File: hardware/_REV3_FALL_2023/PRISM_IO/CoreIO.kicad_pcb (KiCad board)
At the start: 2 copper layers, 61 x 88.9 mm, 39 parts, among them J1 CORE_FC, J2 COTS_SWITCH_PLUG, J3 PYRO 1, J4 PYRO 2, Q1 AO3400A, Q2 AO3400A

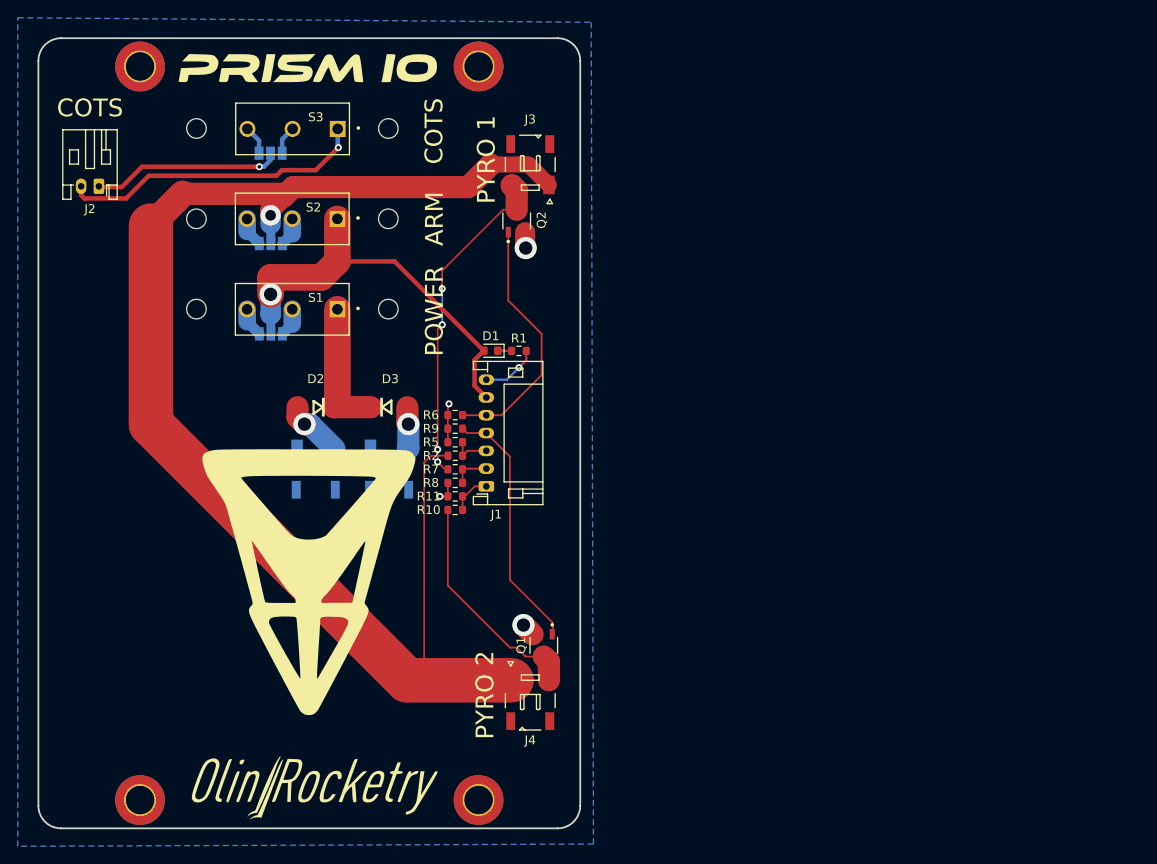
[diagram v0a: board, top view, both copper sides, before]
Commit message: update Core IO schematic and first layout concept
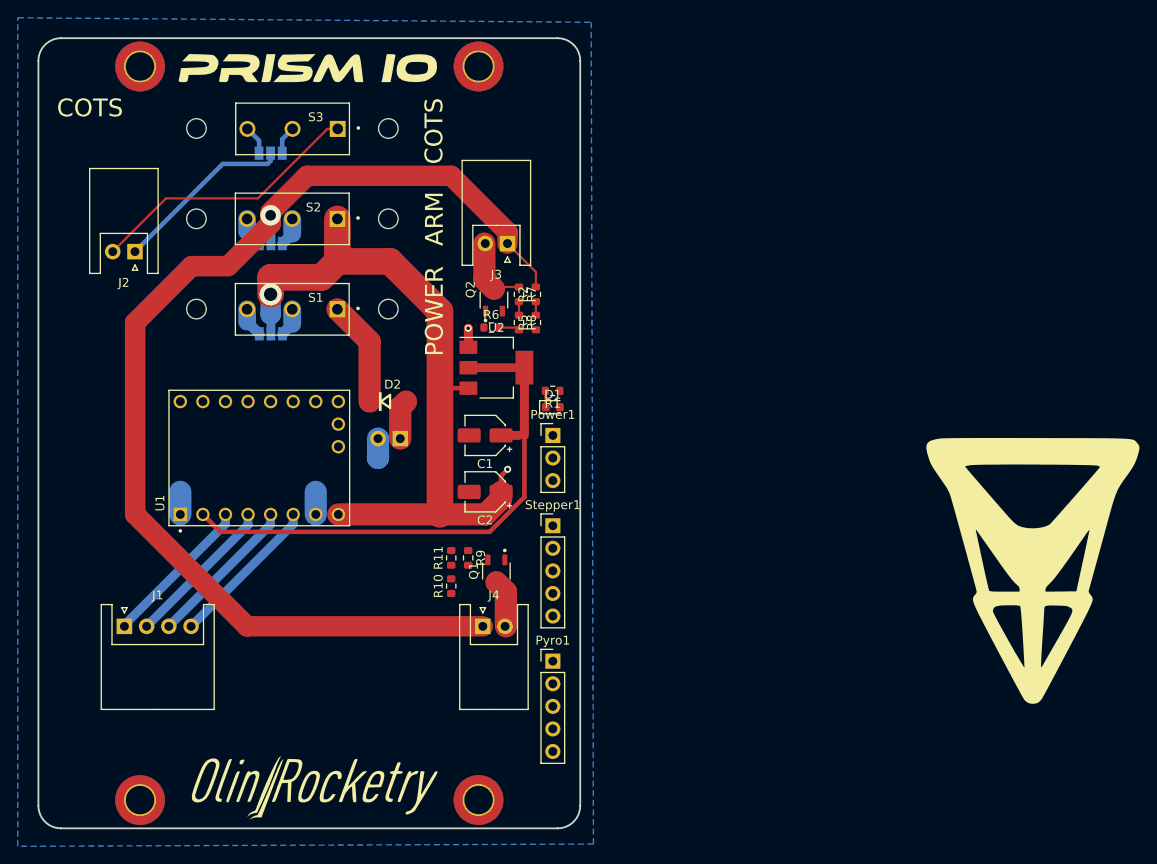
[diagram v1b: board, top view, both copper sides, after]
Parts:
- removed BT2: ~, JST:JST_SFH_SM02B-SFHRS-TF_02x1.80mm_Angled
- removed D3: SS54, JLC_footprints:DO-214AC
- added C1: 10uF, Capacitor_SMD:CP_Elec_4x5.4, F.Cu at (167.6, 95.2)
- added C2: 10uF, Capacitor_SMD:CP_Elec_4x5.4, F.Cu at (167.6, 101.6)
- added Power1: Conn_01x03_Socket, Connector_PinHeader_2.54mm:PinHeader_1x03_P2.54mm_Vertical, F.Cu at (175.3, 95.2)
- added Pyro1: Conn_01x05_Socket, Connector_PinHeader_2.54mm:PinHeader_1x05_P2.54mm_Vertical, F.Cu at (175.3, 120.7)
- added Stepper1: Conn_01x05_Socket, Connector_PinHeader_2.54mm:PinHeader_1x05_P2.54mm_Vertical, F.Cu at (175.3, 105.4)
- added U1: TMC2209_SILENTSTEPSTICK, TMC2209_SILENTSTEPSTICK:MODULE_TMC2209_SILENTSTEPSTICK, F.Cu at (142.2, 97.8)
- added U2: LD1117S12TR_SOT223, Package_TO_SOT_SMD:SOT-223-3_TabPin2, F.Cu at (168.9, 87.6)
- BT1, J3, J4: footprint JST:JST_SFH_SM02B-SFHRS-TF_02x1.80mm_Angled -> Connectors_JST.pretty-master:JST_XH_S02B-XH-A_02x2.50mm_Angled
- J1: value CORE_FC -> Conn_01x04_Socket; footprint Connector_JST:JST_PH_S7B-PH-K_1x07_P2.00mm_Horizontal -> Connectors_JST.pretty-master:JST_XH_S04B-XH-A_04x2.50mm_Angled
- J2: footprint Connector_JST:JST_PH_S2B-PH-K_1x02_P2.00mm_Horizontal -> Connectors_JST.pretty-master:JST_XH_S02B-XH-A_02x2.50mm_Angled
- Q2: footprint AO3400A:SOT95P280X125-3N -> AO3400A.pretty-master:SOT95P280X125-3N
- R1: value 150 -> 1k
- R10: value 10k -> 56K
- R11, R8: value 10k -> 15K
- R2: value 10k -> 56k
- R5: value 10k -> 15k
- moved G*** 81.5 mm to (229.2, 110.5)
- moved J1 43.7 mm to (127.1, 116.7), turned to 0 degrees
- moved R7 21.0 mm to (171.4, 79.4), turned to -90 degrees
- moved R2 20.3 mm to (173.4, 79.4), turned to 90 degrees
- moved R8 19.4 mm to (171.4, 82.5), turned to -90 degrees
- moved R5 16.2 mm to (173.4, 82.5), turned to 90 degrees
- moved R9 14.6 mm to (165.7, 109.0), turned to -90 degrees
- moved R6 10.7 mm to (168.3, 83.1), turned to 0 degrees
- moved BT1 10.1 mm to (158.1, 95.6)
- moved J4 9.92 mm to (167.4, 116.7)
- moved Q1 9.92 mm to (168.9, 110.5)
- moved D1 9.43 mm to (175.3, 92.1), turned to 0 degrees
- moved J3 9.25 mm to (170.2, 73.7)
- moved Q2 9.25 mm to (168.6, 80.0)
- moved R10 8.58 mm to (163.8, 112.2), turned to 90 degrees
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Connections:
- J1 pad 1: /CONT 2 -> Net-(J1-Pin_1)
- J1 pad 2: /CONT 1 -> Net-(J1-Pin_2)
- J1 pad 3: /ARM -> Net-(J1-Pin_3)
- J1 pad 4: /PYRO 2 -> Net-(J1-Pin_4)
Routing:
- net /5V: track 0.00 -> 62.1 mm
- net /V_BATT: track 46.0 -> 81.8 mm, vias 1 -> 2
- net /V_IGNITOR: track 159.4 -> 128.7 mm
- net Net-(J3-Pin_2): track 37.5 -> 8.44 mm, vias 4 -> 0
- net /PYRO 2: track 28.6 -> 0.00 mm
- net /PYRO 1: track 28.4 -> 0.25 mm
- net Net-(J4-Pin_2): track 25.5 -> 5.41 mm
- net Net-(J1-Pin_4): track 0.00 -> 17.3 mm
- net Net-(J1-Pin_3): track 0.00 -> 17.3 mm
- net Net-(J1-Pin_2): track 0.00 -> 17.3 mm
- net Net-(J1-Pin_1): track 0.00 -> 17.3 mm
- net GND: track 16.8 -> 11.8 mm, vias 5 -> 1
- net Net-(BT2-Pad1): track 4.75 -> 0.00 mm, vias 1 -> 0
- net /CONT 2: track 4.67 -> 0.00 mm
- net Net-(J2-Pin_2): track 34.6 -> 31.0 mm, vias 1 -> 0
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
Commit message: fixed stepper wiring
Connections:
- U1 pad 16: unconnected-(U1-~{EN}-Pad16) -> GND
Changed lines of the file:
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@@
   (net 32 "unconnected-(U1-MS2-Pad14)")
   (net 33 "unconnected-(U1-MS1-Pad15)")
-  (net 34 "unconnected-(U1-~{EN}-Pad16)")
-  (net 35 "unconnected-(U1-DIAG-Pad18)")
-  (net 36 "unconnected-(U1-INDEX-Pad17)")
-  (net 37 "/RX 4")
-  (net 38 "/EN")
+  (net 34 "unconnected-(U1-DIAG-Pad18)")
+  (net 35 "unconnected-(U1-INDEX-Pad17)")
+  (net 36 "/RX 4")
+  (net 37 "/EN")
   (footprint "AO3400A.pretty-master:SOT95P280X125-3N" (layer "F.Cu")
     (at 168.636 80.01 90)
@@
       (stroke (width 0.1) (type solid)) (layer "F.Fab"))
     (pad "1" thru_hole rect (at 0 0) (size 1.7 1.7) (drill 1) (layers "*.Cu" "*.Mask")
-      (net 37 "/RX 4") (pinfunction "Pin_1") (pintype "passive"))
+      (net 36 "/RX 4") (pinfunction "Pin_1") (pintype "passive"))
     (pad "2" thru_hole oval (at 0 2.54) (size 1.7 1.7) (drill 1) (layers "*.Cu" "*.Mask")
       (net 30 "/UART") (pinfunction "Pin_2") (pintype "passive"))
     (pad "3" thru_hole oval (at 0 5.08) (size 1.7 1.7) (drill 1) (layers "*.Cu" "*.Mask")
-      (net 38 "/EN") (pinfunction "Pin_3") (pintype "passive"))
+      (net 37 "/EN") (pinfunction "Pin_3") (pintype "passive"))
     (pad "4" thru_hole oval (at 0 7.62) (size 1.7 1.7) (drill 1) (layers "*.Cu" "*.Mask")
       (net 27 "/DIR") (pinfunction "Pin_4") (pintype "passive"))
@@
       (net 33 "unconnected-(U1-MS1-Pad15)") (pinfunction "MS1") (pintype "input+no_connect") (solder_mask_margin 0.102))
     (pad "16" thru_hole circle (at 6.35 8.89 90) (size 1.508 1.508) (drill 1) (layers "*.Cu" "*.Mask")
-      (net 34 "unconnected-(U1-~{EN}-Pad16)") (pinfunction "~{EN}") (pintype "input+no_connect") (solder_mask_margin 0.102))
+      (net 7 "GND") (pinfunction "~{EN}") (pintype "input") (solder_mask_margin 0.102))
     (pad "17" thru_hole circle (at 1.27 8.89 90) (size 1.508 1.508) (drill 1) (layers "*.Cu" "*.Mask")
-      (net 36 "unconnected-(U1-INDEX-Pad17)") (pinfunction "INDEX") (pintype "output+no_connect") (solder_mask_margin 0.102))
+      (net 35 "unconnected-(U1-INDEX-Pad17)") (pinfunction "INDEX") (pintype "output+no_connect") (solder_mask_margin 0.102))
     (pad "18" thru_hole circle (at 3.81 8.89 90) (size 1.508 1.508) (drill 1) (layers "*.Cu" "*.Mask")
-      (net 35 "unconnected-(U1-DIAG-Pad18)") (pinfunction "DIAG") (pintype "output+no_connect") (solder_mask_margin 0.102))
+      (net 34 "unconnected-(U1-DIAG-Pad18)") (pinfunction "DIAG") (pintype "output+no_connect") (solder_mask_margin 0.102))
   )
   (footprint "MountingHole:MountingHole_2.2mm_M2" (layer "F.Cu")

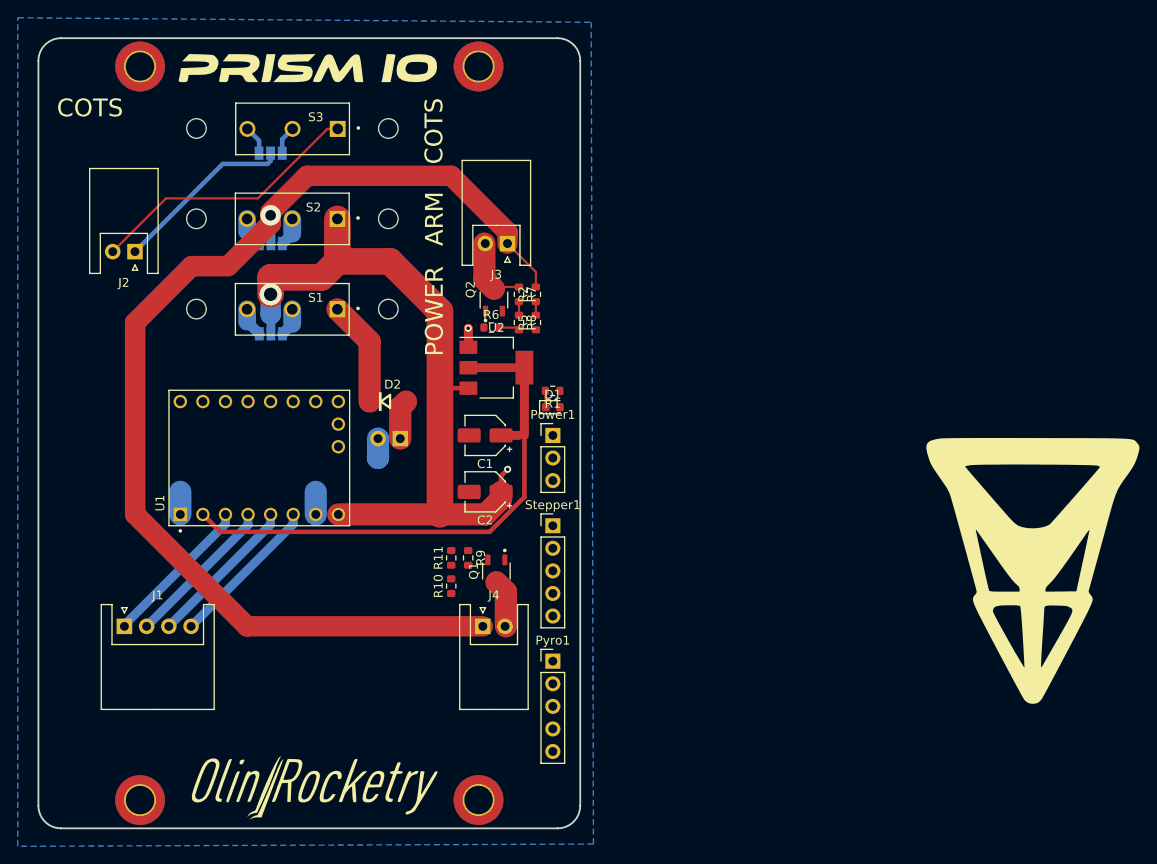
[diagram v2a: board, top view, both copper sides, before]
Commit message: finished IO layout
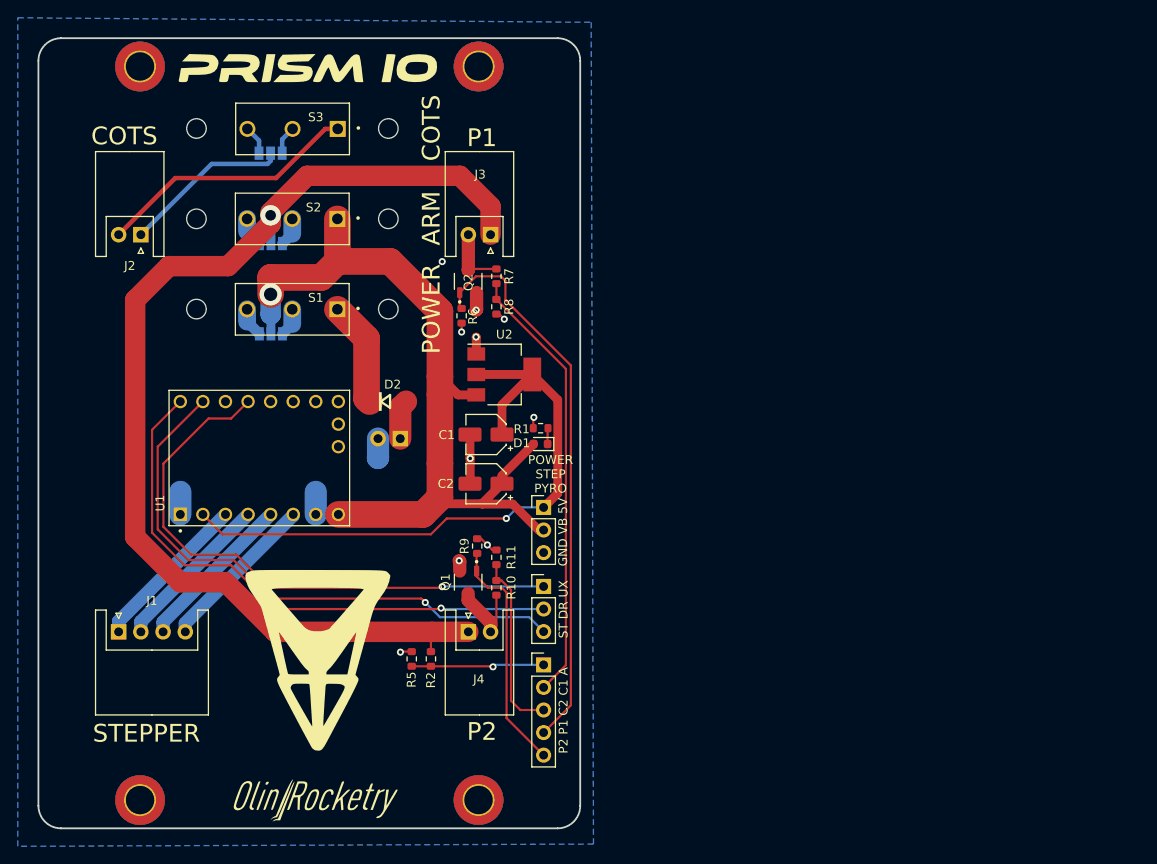
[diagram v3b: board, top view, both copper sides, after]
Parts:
- removed the ? at (148.3, 134.6)
- removed the G*** at (229.2, 110.5)
- removed Power1: Conn_01x03_Socket, Connector_PinHeader_2.54mm:PinHeader_1x03_P2.54mm_Vertical
- removed Pyro1, Stepper1: Conn_01x05_Socket, Connector_PinHeader_2.54mm:PinHeader_1x05_P2.54mm_Vertical
- added G***: LOGO, LOGO, F.Cu at (148.8, 120.5)
- added G***: LOGO, LOGO, F.Cu at (148.5, 136.1)
- added Power2: Conn_01x03_Socket, Connector_PinHeader_2.54mm:PinHeader_1x03_P2.54mm_Vertical, F.Cu at (174.2, 103.4)
- added Pyro2: Conn_01x05_Socket, Connector_PinHeader_2.54mm:PinHeader_1x05_P2.54mm_Vertical, F.Cu at (174.2, 121.1)
- added Stepper2: Conn_01x03_Socket, Connector_PinHeader_2.54mm:PinHeader_1x03_P2.54mm_Vertical, F.Cu at (174.2, 112.2)
- moved R2 42.7 mm to (161.5, 120.4)
- moved R5 40.3 mm to (159.4, 120.4), turned to -90 degrees
- moved R10 5.08 mm to (168.9, 112.4)
- moved R11 5.08 mm to (168.9, 109.0)
- moved R1 4.41 mm to (173.9, 94.4), turned to 0 degrees
- moved D1 4.36 mm to (173.9, 96.2), turned to 180 degrees
- moved R6 3.59 mm to (165.0, 81.8), turned to -90 degrees
- moved Q2 3.58 mm to (165.7, 77.9)
- moved Q1 3.41 mm to (165.7, 111.8)
- moved R7 3.25 mm to (168.9, 77.3)
- moved R8 3.10 mm to (168.9, 80.8)
- moved J3 2.15 mm to (168.3, 72.7)
- moved J2 2.02 mm to (128.9, 72.7)
- moved J4 1.75 mm to (165.8, 117.3)
- moved R9 1.68 mm to (166.8, 107.7), turned to 90 degrees
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- renumbered BT1 to BATT
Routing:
- net /UART: track 0.00 -> 65.2 mm, vias 0 -> 1
- net /STEP: track 0.00 -> 64.7 mm, vias 0 -> 1
- net /DIR: track 0.00 -> 63.8 mm, vias 0 -> 1
- net /PYRO 1: track 0.25 -> 63.1 mm
- net /CONT 1: track 1.52 -> 49.7 mm
- net /PYRO 2: track 0.00 -> 26.8 mm
- net /CONT 2: track 0.00 -> 20.4 mm
- net GND: track 11.8 -> 25.3 mm, vias 1 -> 10
- net /ARM: track 1.52 -> 15.0 mm, vias 0 -> 1
- net /V_BATT: track 81.8 -> 94.2 mm, vias 2 -> 1
- net /5V: track 62.1 -> 72.8 mm, vias 0 -> 1
- net Net-(J4-Pin_2): track 5.41 -> 9.78 mm
- net /V_IGNITOR: track 128.7 -> 125.2 mm
- net Net-(J2-Pin_2): track 31.0 -> 29.6 mm
- net Net-(J3-Pin_2): track 8.44 -> 7.24 mm
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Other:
- board text added: "GND VB 5V"
- board text added: "P1"
- board text added: "P2"
- board text added: "P2 P1 C2 C1 A"
- board text added: "POWER STEP PYRO"
- board text added: "ST DR UX"
- board text added: "STEPPER"

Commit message: Add aesthetics to IO board
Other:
- board text added: "Alex Mineeva"
- board text added: "Ari Bobesh"
- board text added: "DESIGN BY"
- board text added: "Daniel Theunissen"
- board text added: "Ertug Umsur"
- board text added: "Ishan Porwal"
- board text added: "Joseph Liu"
- board text added: "Mateo Brancoli"
- board text added: "Nividh Singh"
- board text added: "Rohan Shah"
- board text added: "Rowan Jansens"
- board text removed: "Ari Bobesh Charlie Babe Jiayuan Liu Lili Baker Rowan Jansens"

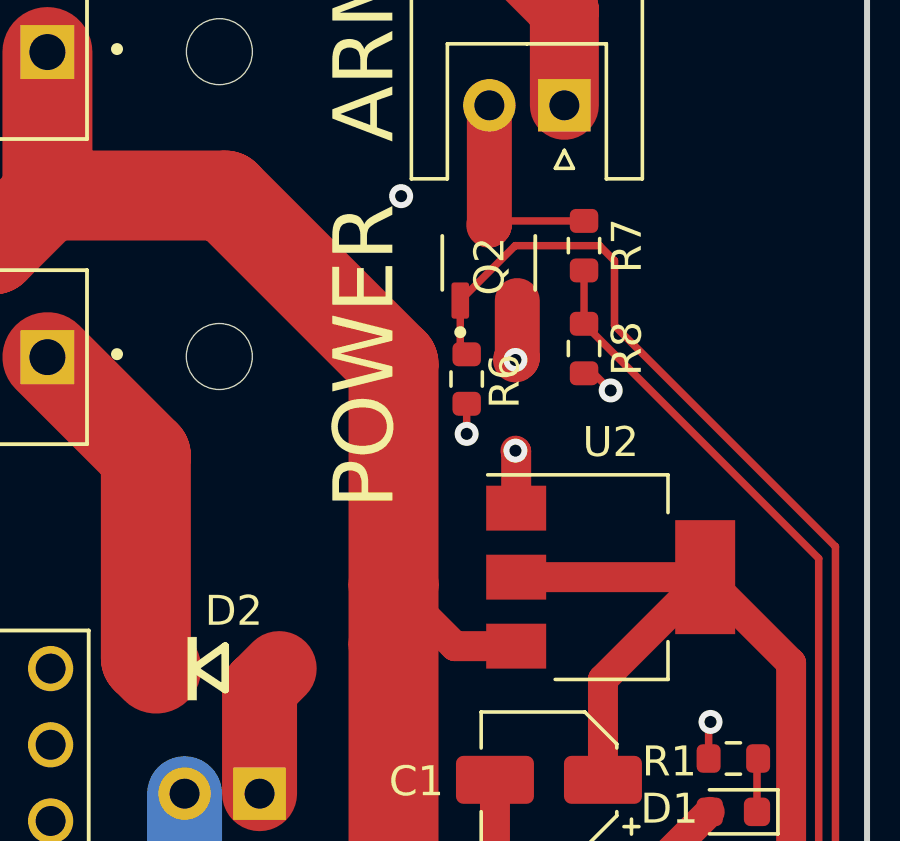
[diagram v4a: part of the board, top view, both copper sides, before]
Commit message: Change IO pulldown resistors
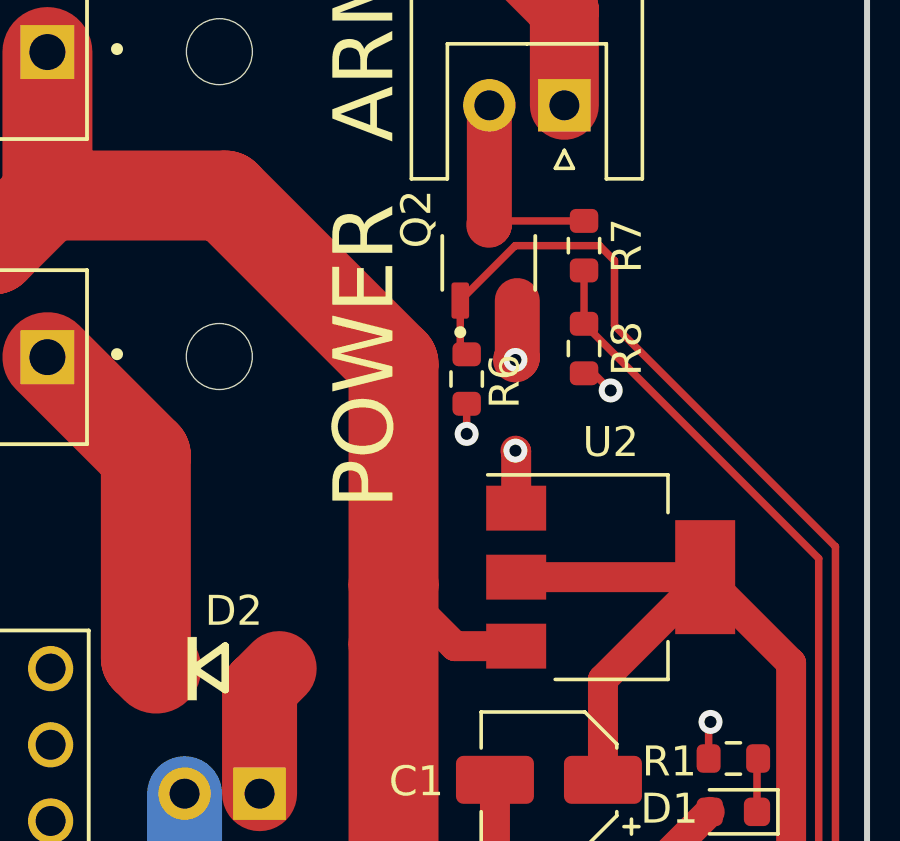
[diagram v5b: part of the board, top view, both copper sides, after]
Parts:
- Q2: footprint AO3400A.pretty-master:SOT95P280X125-3N -> rocketry_footprints:SOT95P280X125-3N
- R6, R9: value 1M -> 10k
- R7: value 10k -> 56k
- renumbered BATT to BT1
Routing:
- net GND: vias 10 -> 9
